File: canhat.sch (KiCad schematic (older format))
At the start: 21 parts, among them J1 Raspberry_Pi_2_3, J2 CAN In, J3 CAN Out, U1 MCP2515-xSO, U2 MCP2551-I-SN, U3 AT24C32-SSHM, Y1 16MHz

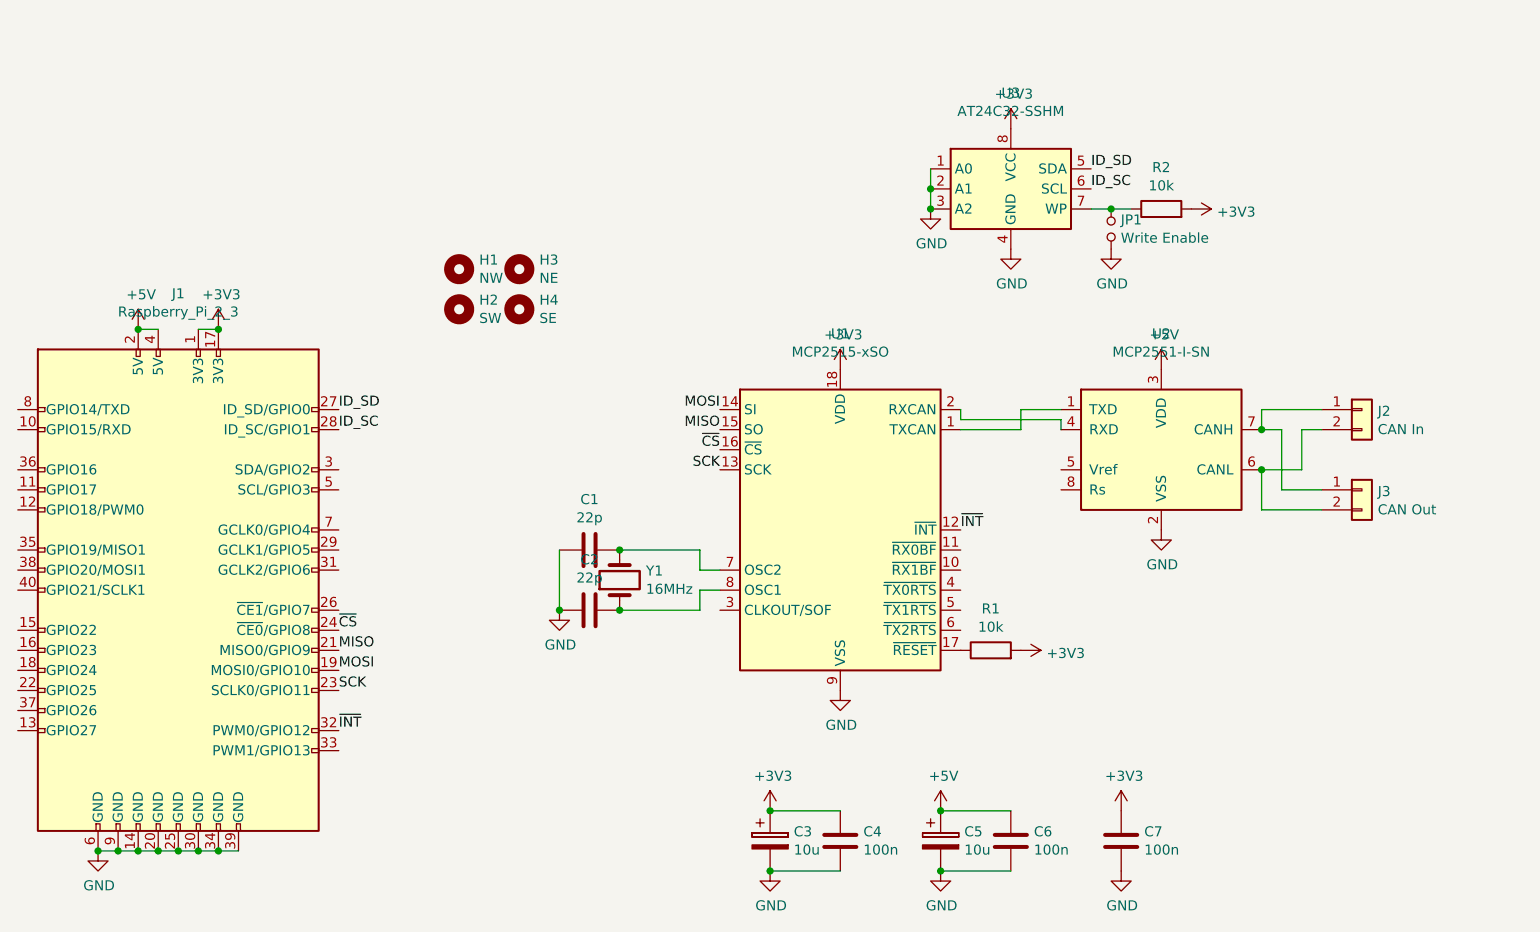
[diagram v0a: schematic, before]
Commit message: Added I2C pullups and CAN microstrip
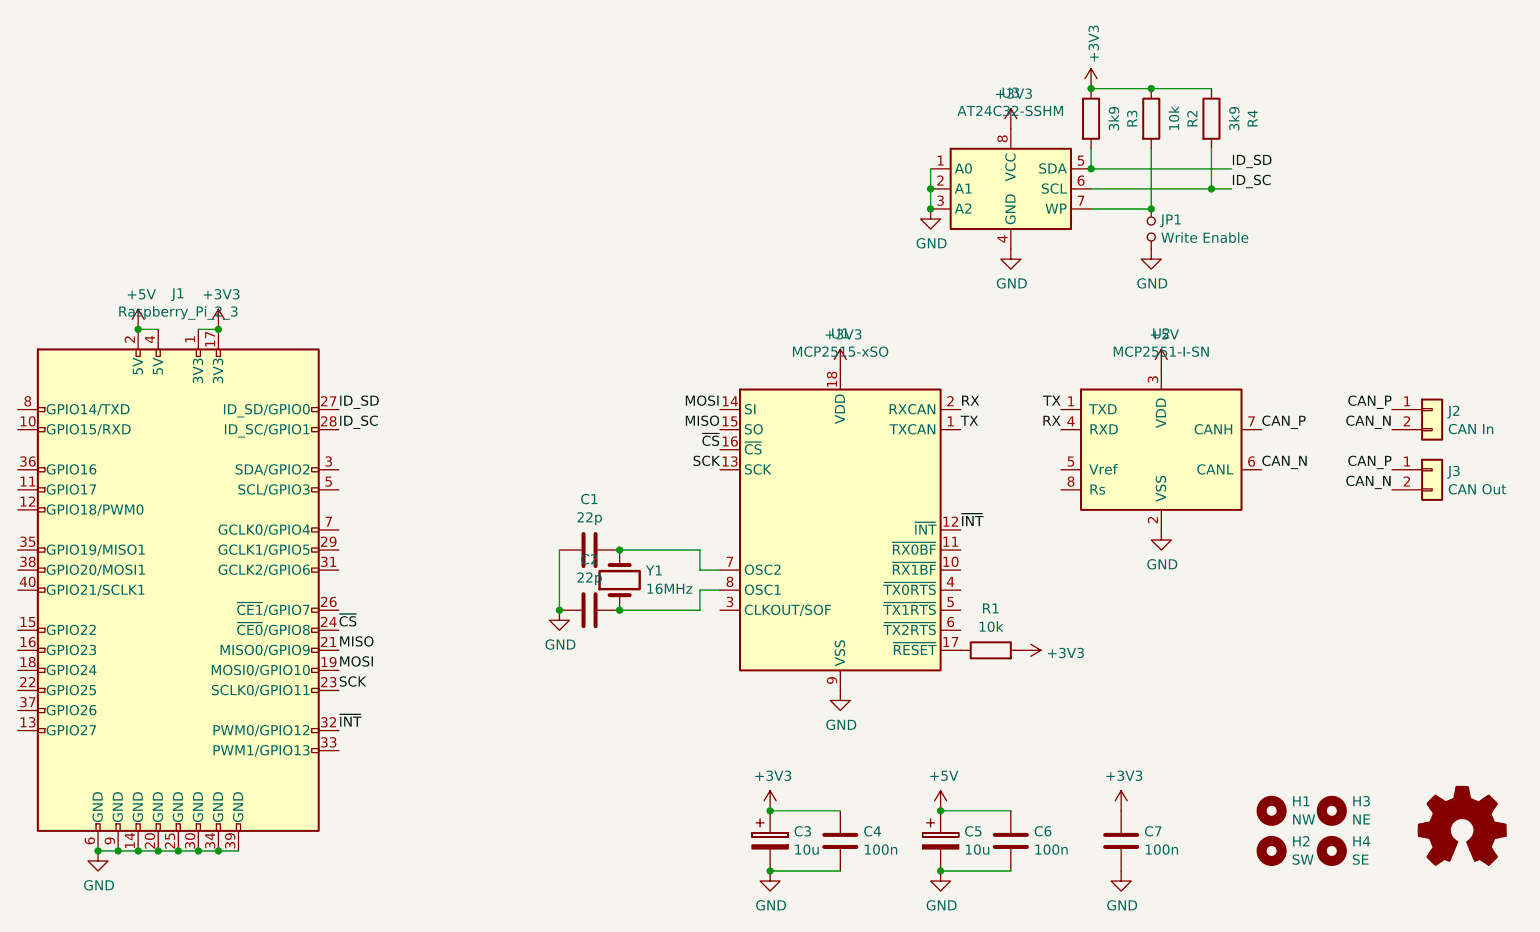
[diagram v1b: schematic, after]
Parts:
- added OSHW1: Logo_Open_Hardware_Small, Symbol:OSHW-Logo_5.7x6mm_SilkScreen, symbol Graphic:Logo_Open_Hardware_Small
- added R3, R4: 3k9, Resistor_SMD:R_0805_2012Metric_Pad1.15x1.40mm_HandSolder, symbol Device:R
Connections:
- net +3V3: now also R2.1, R3.1, R4.1; no longer R2.2
- net ID_SC: now also R4.2
- net ID_SD: now also R3.2
- net TX: now reaches U1.1 (TXCAN), U2.1 (TXD)
- net RX: now reaches U1.2 (RXCAN), U2.4 (RXD)
- net CAN_N: now reaches J2.2 (Pin_2), J3.2 (Pin_2), U2.6 (CANL)
- net CAN_P: now reaches J2.1 (Pin_1), J3.1 (Pin_1), U2.7 (CANH)
- net at JP1.1, U3.7 (WP): now also R2.2; no longer R2.1
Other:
- moved on the sheet: H1, H2, H3, H4, J2, J3, JP1, R2
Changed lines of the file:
@@
 EESchema Schematic File Version 4
+LIBS:canhat-cache
 EELAYER 26 0
 EELAYER END
@@
 encoding utf-8
 Sheet 1 1
-Title ""
-Date ""
-Rev ""
-Comp ""
+Title "CAN HAT"
+Date "2019-04-02"
+Rev "1"
+Comp "© 2019 Gregor Riepl"
 Comment1 ""
 Comment2 ""
@@
 L Connector_Generic:Conn_01x02 J2
 U 1 1 5CA2AC48
-P 9100 3200
-F 0 "J2" H 9179 3192 50  0000 L CNN
-F 1 "CAN In" H 9179 3101 50  0000 L CNN
-F 2 "TerminalBlock_TE-Connectivity:TerminalBlock_TE_282834-2_1x02_P2.54mm_Horizontal" H 9100 3200 50  0001 C CNN
-F 3 "~" H 9100 3200 50  0001 C CNN
-	1    9100 3200
+P 9450 3200
+F 0 "J2" H 9529 3192 50  0000 L CNN
+F 1 "CAN In" H 9529 3101 50  0000 L CNN
+F 2 "TerminalBlock_TE-Connectivity:TerminalBlock_TE_282834-2_1x02_P2.54mm_Horizontal" H 9450 3200 50  0001 C CNN
+F 3 "~" H 9450 3200 50  0001 C CNN
+	1    9450 3200
 	1    0    0    -1
 $EndComp
@@
 L Connector_Generic:Conn_01x02 J3
 U 1 1 5CA2B324
-P 9100 3600
-F 0 "J3" H 9179 3592 50  0000 L CNN
-F 1 "CAN Out" H 9179 3501 50  0000 L CNN
-F 2 "TerminalBlock_TE-Connectivity:TerminalBlock_TE_282834-2_1x02_P2.54mm_Horizontal" H 9100 3600 50  0001 C CNN
-F 3 "~" H 9100 3600 50  0001 C CNN
-	1    9100 3600
-	1    0    0    -1
-$EndComp
-Wire Wire Line
-	8900 3200 8600 3200
-Wire Wire Line
-	8600 3200 8600 3300
-Wire Wire Line
-	8600 3300 8700 3300
-Wire Wire Line
-	8700 3300 8700 3600
-Wire Wire Line
-	8700 3600 8900 3600
-Connection ~ 8600 3300
-Wire Wire Line
-	8600 3500 8600 3700
-Wire Wire Line
-	8600 3700 8900 3700
-Wire Wire Line
-	8600 3500 8800 3500
-Wire Wire Line
-	8800 3500 8800 3300
-Wire Wire Line
-	8800 3300 8900 3300
-Connection ~ 8600 3500
-Wire Wire Line
-	7100 3200 7100 3250
-Wire Wire Line
-	7100 3250 7600 3250
-Wire Wire Line
-	7600 3250 7600 3300
-Wire Wire Line
-	7100 3300 7400 3300
-Wire Wire Line
-	7400 3300 7400 3200
-Wire Wire Line
-	7400 3200 7600 3200
+P 9450 3500
+F 0 "J3" H 9529 3492 50  0000 L CNN
+F 1 "CAN Out" H 9529 3401 50  0000 L CNN
+F 2 "TerminalBlock_TE-Connectivity:TerminalBlock_TE_282834-2_1x02_P2.54mm_Horizontal" H 9450 3500 50  0001 C CNN
+F 3 "~" H 9450 3500 50  0001 C CNN
+	1    9450 3500
+	1    0    0    -1
+$EndComp
 $Comp
 L Mechanical:MountingHole H1
 U 1 1 5CA2E828
-P 4600 2500
-F 0 "H1" H 4700 2546 50  0000 L CNN
-F 1 "NW" H 4700 2455 50  0000 L CNN
-F 2 "MountingHole:MountingHole_2.7mm" H 4600 2500 50  0001 C CNN
-F 3 "~" H 4600 2500 50  0001 C CNN
-	1    4600 2500
+P 8650 5200
+F 0 "H1" H 8750 5246 50  0000 L CNN
+F 1 "NW" H 8750 5155 50  0000 L CNN
+F 2 "MountingHole:MountingHole_2.7mm" H 8650 5200 50  0001 C CNN
+F 3 "~" H 8650 5200 50  0001 C CNN
+	1    8650 5200
 	1    0    0    -1
 $EndComp
@@
 L Mechanical:MountingHole H3
 U 1 1 5CA2E89E
-P 4900 2500
-F 0 "H3" H 5000 2546 50  0000 L CNN
-F 1 "NE" H 5000 2455 50  0000 L CNN
-F 2 "MountingHole:MountingHole_2.7mm" H 4900 2500 50  0001 C CNN
-F 3 "~" H 4900 2500 50  0001 C CNN
-	1    4900 2500
+P 8950 5200
+F 0 "H3" H 9050 5246 50  0000 L CNN
+F 1 "NE" H 9050 5155 50  0000 L CNN
+F 2 "MountingHole:MountingHole_2.7mm" H 8950 5200 50  0001 C CNN
+F 3 "~" H 8950 5200 50  0001 C CNN
+	1    8950 5200
 	1    0    0    -1
 $EndComp
@@
 L Mechanical:MountingHole H2
 U 1 1 5CA2E8D0
-P 4600 2700
-F 0 "H2" H 4700 2746 50  0000 L CNN
-F 1 "SW" H 4700 2655 50  0000 L CNN
-F 2 "MountingHole:MountingHole_2.7mm" H 4600 2700 50  0001 C CNN
-F 3 "~" H 4600 2700 50  0001 C CNN
-	1    4600 2700
+P 8650 5400
+F 0 "H2" H 8750 5446 50  0000 L CNN
+F 1 "SW" H 8750 5355 50  0000 L CNN
+F 2 "MountingHole:MountingHole_2.7mm" H 8650 5400 50  0001 C CNN
+F 3 "~" H 8650 5400 50  0001 C CNN
+	1    8650 5400
 	1    0    0    -1
 $EndComp
@@
 L Mechanical:MountingHole H4
 U 1 1 5CA2E904
-P 4900 2700
-F 0 "H4" H 5000 2746 50  0000 L CNN
-F 1 "SE" H 5000 2655 50  0000 L CNN
-F 2 "MountingHole:MountingHole_2.7mm" H 4900 2700 50  0001 C CNN
-F 3 "~" H 4900 2700 50  0001 C CNN
-	1    4900 2700
+P 8950 5400
+F 0 "H4" H 9050 5446 50  0000 L CNN
+F 1 "SE" H 9050 5355 50  0000 L CNN
+F 2 "MountingHole:MountingHole_2.7mm" H 8950 5400 50  0001 C CNN
+F 3 "~" H 8950 5400 50  0001 C CNN
+	1    8950 5400
 	1    0    0    -1
 $EndComp
@@
 L Device:R R2
 U 1 1 5CA2F18E
-P 8100 2200
-F 0 "R2" V 8307 2200 50  0000 C CNN
-F 1 "10k" V 8216 2200 50  0000 C CNN
-F 2 "Resistor_SMD:R_0805_2012Metric_Pad1.15x1.40mm_HandSolder" V 8030 2200 50  0001 C CNN
-F 3 "~" H 8100 2200 50  0001 C CNN
-	1    8100 2200
-	0    -1   -1   0
-$EndComp
-$Comp
-L power:+3V3 #PWR07
-U 1 1 5CA2F1FE
-P 8250 2200
-F 0 "#PWR07" H 8250 2050 50  0001 C CNN
-F 1 "+3V3" V 8265 2328 50  0000 L CNN
-F 2 "" H 8250 2200 50  0001 C CNN
-F 3 "" H 8250 2200 50  0001 C CNN
-	1    8250 2200
-	0    1    1    0
+P 8050 1750
+F 0 "R2" V 8257 1750 50  0000 C CNN
+F 1 "10k" V 8166 1750 50  0000 C CNN
+F 2 "Resistor_SMD:R_0805_2012Metric_Pad1.15x1.40mm_HandSolder" V 7980 1750 50  0001 C CNN
+F 3 "~" H 8050 1750 50  0001 C CNN
+	1    8050 1750
+	1    0    0    -1
 $EndComp
 $Comp
 L Device:Jumper_NO_Small JP1
 U 1 1 5CA2F52A
-P 7850 2300
-F 0 "JP1" V 7804 2348 50  0000 L CNN
-F 1 "Write Enable" V 7895 2348 50  0000 L CNN
-F 2 "Connector_PinHeader_2.54mm:PinHeader_1x02_P2.54mm_Vertical" H 7850 2300 50  0001 C CNN
-F 3 "~" H 7850 2300 50  0001 C CNN
-	1    7850 2300
+P 8050 2300
+F 0 "JP1" V 8004 2348 50  0000 L CNN
+F 1 "Write Enable" V 8095 2348 50  0000 L CNN
+F 2 "Connector_PinHeader_2.54mm:PinHeader_1x02_P2.54mm_Vertical" H 8050 2300 50  0001 C CNN
+F 3 "~" H 8050 2300 50  0001 C CNN
+	1    8050 2300
 	0    1    1    0
 $EndComp
-Text Label 7750 2100 0    50   ~ 0
+Text Label 8450 2100 0    50   ~ 0
 ID_SC
-Text Label 7750 2000 0    50   ~ 0
+Text Label 8450 2000 0    50   ~ 0
 ID_SD
 Text Label 4000 3200 0    50   ~ 0
@@
 ID_SC
 Wire Wire Line
-	7750 2200 7850 2200
-Connection ~ 7850 2200
-Wire Wire Line
-	7850 2200 7950 2200
+	8050 2200 8050 1900
 $Comp
 L power:GND #PWR03
@@
 L power:GND #PWR04
 U 1 1 5CA2FDC6
-P 7850 2400
-F 0 "#PWR04" H 7850 2150 50  0001 C CNN
-F 1 "GND" H 7855 2227 50  0000 C CNN
-F 2 "" H 7850 2400 50  0001 C CNN
-F 3 "" H 7850 2400 50  0001 C CNN
-	1    7850 2400
+P 8050 2400
+F 0 "#PWR04" H 8050 2150 50  0001 C CNN
+F 1 "GND" H 8055 2227 50  0000 C CNN
+F 2 "" H 8050 2400 50  0001 C CNN
+F 3 "" H 8050 2400 50  0001 C CNN
+	1    8050 2400
 	1    0    0    -1
 $EndComp
@@
 	1    0    0    -1
 $EndComp
+$Comp
+L Device:R R3
+U 1 1 5CA302D1
+P 7750 1750
+F 0 "R3" V 7957 1750 50  0000 C CNN
+F 1 "3k9" V 7866 1750 50  0000 C CNN
+F 2 "Resistor_SMD:R_0805_2012Metric_Pad1.15x1.40mm_HandSolder" V 7680 1750 50  0001 C CNN
+F 3 "~" H 7750 1750 50  0001 C CNN
+	1    7750 1750
+	1    0    0    -1
+$EndComp
+$Comp
+L Device:R R4
+U 1 1 5CA30AE7
+P 8350 1750
+F 0 "R4" V 8557 1750 50  0000 C CNN
+F 1 "3k9" V 8466 1750 50  0000 C CNN
+F 2 "Resistor_SMD:R_0805_2012Metric_Pad1.15x1.40mm_HandSolder" V 8280 1750 50  0001 C CNN
+F 3 "~" H 8350 1750 50  0001 C CNN
+	1    8350 1750
+	1    0    0    -1
+$EndComp
+Wire Wire Line
+	7750 2000 7750 1900
+Wire Wire Line
+	7750 2100 8350 2100
+Wire Wire Line
+	8350 2100 8350 1900
+Wire Wire Line
+	7750 2000 8450 2000
+Connection ~ 7750 2000
+Wire Wire Line
+	8350 2100 8450 2100
+Connection ~ 8350 2100
+$Comp
+L power:+3V3 #PWR08
+U 1 1 5CA33262
+P 7750 1600
+F 0 "#PWR08" H 7750 1450 50  0001 C CNN
+F 1 "+3V3" V 7765 1728 50  0000 L CNN
+F 2 "" H 7750 1600 50  0001 C CNN
+F 3 "" H 7750 1600 50  0001 C CNN
+	1    7750 1600
+	1    0    0    -1
+$EndComp
+Wire Wire Line
+	7750 1600 8050 1600
+Connection ~ 7750 1600
+Connection ~ 8050 1600
+Wire Wire Line
+	8050 1600 8350 1600
+Connection ~ 8050 2200
+Wire Wire Line
+	7750 2200 8050 2200
+$Comp
+L Graphic:Logo_Open_Hardware_Small OSHW1
+U 1 1 5CA3B81F
+P 9600 5300
+F 0 "OSHW1" H 9600 5575 50  0001 C CNN
+F 1 "Logo_Open_Hardware_Small" H 9600 5075 50  0001 C CNN
+F 2 "Symbol:OSHW-Logo_5.7x6mm_SilkScreen" H 9600 5300 50  0001 C CNN
+F 3 "~" H 9600 5300 50  0001 C CNN
+	1    9600 5300
+	1    0    0    -1
+$EndComp
+Text Label 7100 3200 0    50   ~ 0
+RX
+Text Label 7600 3300 2    50   ~ 0
+RX
+Text Label 7600 3200 2    50   ~ 0
+TX
+Text Label 7100 3300 0    50   ~ 0
+TX
+Text Label 8600 3300 0    50   ~ 0
+CAN_P
+Text Label 8600 3500 0    50   ~ 0
+CAN_N
+Text Label 9250 3200 2    50   ~ 0
+CAN_P
+Text Label 9250 3500 2    50   ~ 0
+CAN_P
+Text Label 9250 3300 2    50   ~ 0
+CAN_N
+Text Label 9250 3600 2    50   ~ 0
+CAN_N
 $EndSCHEMATC

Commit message: Corrected 1k pullup
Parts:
- R2: value 10k -> 1k
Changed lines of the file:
@@
 P 8050 1750
 F 0 "R2" V 8257 1750 50  0000 C CNN
-F 1 "10k" V 8166 1750 50  0000 C CNN
+F 1 "1k" V 8166 1750 50  0000 C CNN
 F 2 "Resistor_SMD:R_0805_2012Metric_Pad1.15x1.40mm_HandSolder" V 7980 1750 50  0001 C CNN
 F 3 "~" H 8050 1750 50  0001 C CNN
